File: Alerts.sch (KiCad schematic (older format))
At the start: 26 parts, among them J602 Lights, Q601 bss138, Q602 mac97a8, Q603 bss138, Q604 bss138, Q605 mac97a8, Q606 bss138, Q607 mac97a8, U601 4N35, U602 4N35, U603 4N35

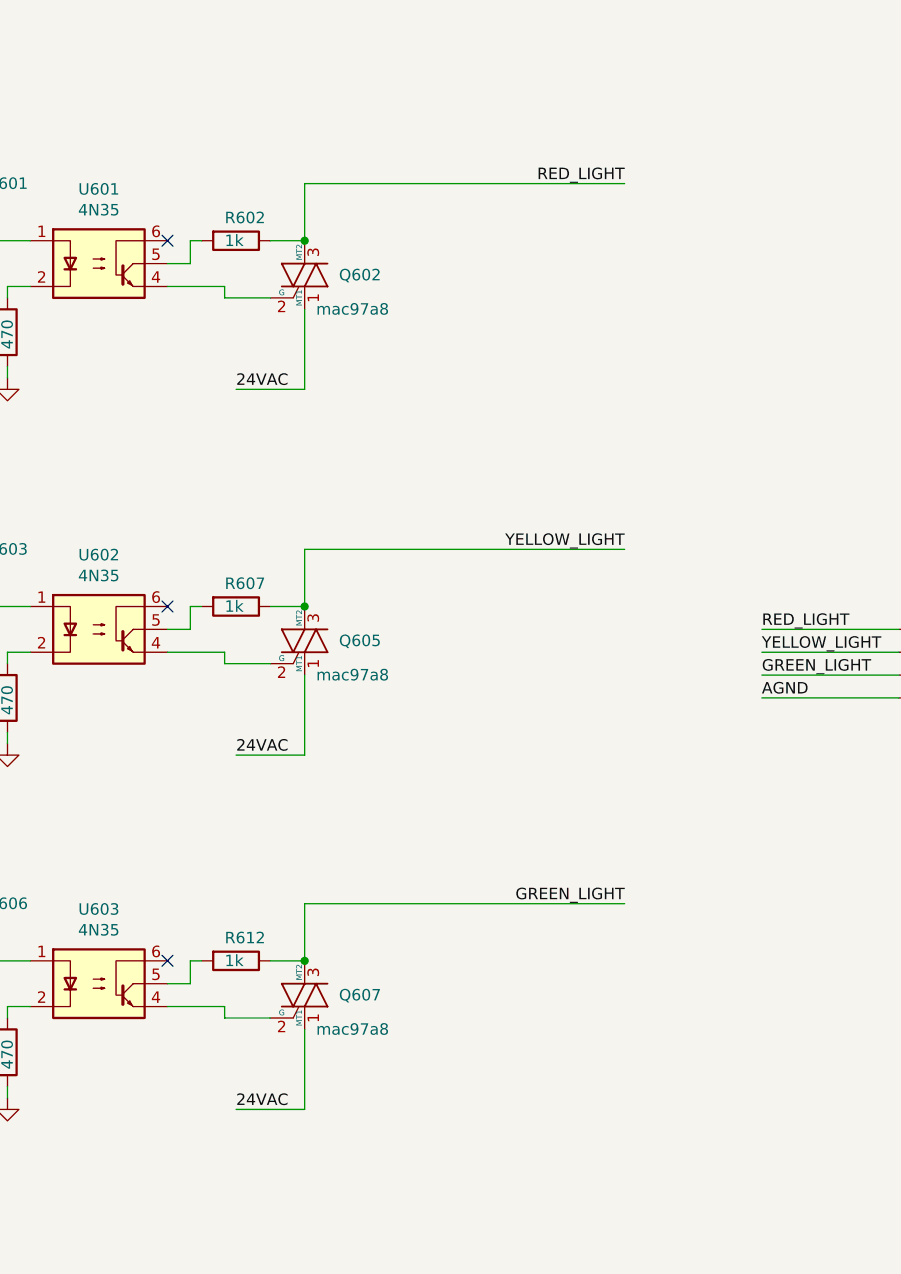
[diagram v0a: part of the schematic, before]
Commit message: Fix por revision grupal
    *Fix de memoria de i2c, mal sda y scl
    *Fix inpunts sda y scl
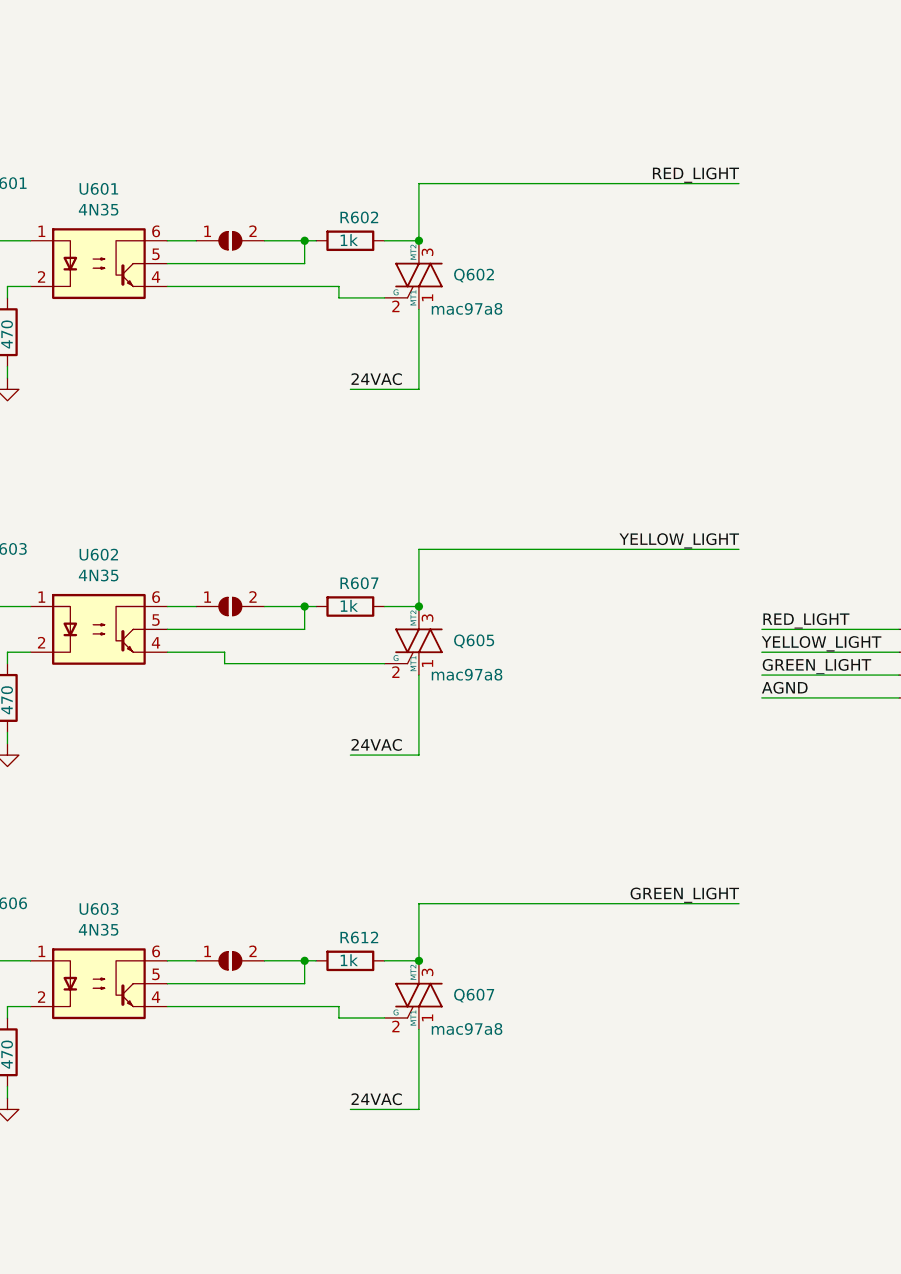
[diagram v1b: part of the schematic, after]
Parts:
- added JP601, JP602, JP603: jumper, 00_lib_fp:SolderJumper-2_P1.3mm_Open_RoundedPad1.0x1.5mm, symbol 00_lib_sch:jumper
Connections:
- net at R602.2, U601.5: now also JP601.2 (B)
- net at U601.6: now also JP601.1 (A)
- net at R607.2, U602.5: now also JP602.2 (B)
- net at U602.6: now also JP602.1 (A)
- net at R612.2, U603.5: now also JP603.2 (B)
- net at U603.6: now also JP603.1 (A)
- no-connect marks 3 -> 0
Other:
- moved on the sheet: Q602, Q605, Q607, R602, R607, R612
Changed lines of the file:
@@
 L 00_lib_sch:Mac97a8 Q?
 U 1 1 616FE40F
-P 7000 1850
+P 7500 1850
 AR Path="/616FE40F" Ref="Q?"  Part="1"
 AR Path="/61410FC3/616FE40F" Ref="Q?"  Part="1"
 AR Path="/61434A7C/616FE40F" Ref="Q?"  Part="1"
 AR Path="/6165BF0A/616FE40F" Ref="Q602"  Part="1"
-F 0 "Q602" H 7150 1850 50  0000 L CNN
-F 1 "mac97a8" H 7050 1700 50  0000 L CNN
-F 2 "00_lib_fp:TO-92_Inline" H 7200 1775 50  0001 L CIN
-F 3 "" H 7000 1850 50  0001 L CNN
-	1    7000 1850
+F 0 "Q602" H 7650 1850 50  0000 L CNN
+F 1 "mac97a8" H 7550 1700 50  0000 L CNN
+F 2 "00_lib_fp:TO-92_Inline" H 7700 1775 50  0001 L CIN
+F 3 "" H 7500 1850 50  0001 L CNN
+	1    7500 1850
 	1    0    0    -1
 $EndComp
@@
 L 00_lib_sch:R R602
 U 1 1 616FE43D
-P 6700 1700
-F 0 "R602" V 6600 1650 50  0000 L CNN
-F 1 "1k" V 6700 1650 50  0000 L CNN
-F 2 "00_lib_fp:R_0805_2012Metric_Pad1.20x1.40mm_HandSolder" V 6630 1700 50  0001 C CNN
-F 3 "~" H 6700 1700 50  0001 C CNN
-	1    6700 1700
+P 7200 1700
+F 0 "R602" V 7100 1650 50  0000 L CNN
+F 1 "1k" V 7200 1650 50  0000 L CNN
+F 2 "00_lib_fp:R_0805_2012Metric_Pad1.20x1.40mm_HandSolder" V 7130 1700 50  0001 C CNN
+F 3 "~" H 7200 1700 50  0001 C CNN
+	1    7200 1700
 	0    1    1    0
 $EndComp
-Wire Wire Line
-	6400 1900 6650 1900
 $Comp
 L 00_lib_sch:GND #PWR?
@@
 $EndComp
 Wire Wire Line
-	6850 1700 7000 1700
-Wire Wire Line
-	7000 1700 7000 1450
-Connection ~ 7000 1700
-Wire Wire Line
-	6650 1900 6650 1950
-Wire Wire Line
-	6650 1950 6850 1950
-Wire Wire Line
-	7000 2000 7000 2350
+	7350 1700 7500 1700
+Wire Wire Line
+	7500 1700 7500 1450
+Connection ~ 7500 1700
+Wire Wire Line
+	7150 1900 7150 1950
+Wire Wire Line
+	7150 1950 7350 1950
+Wire Wire Line
+	7500 2000 7500 2350
 Wire Wire Line
 	5500 2300 5500 2250
@@
 L 00_lib_sch:Mac97a8 Q?
 U 1 1 61703A19
-P 7000 3450
+P 7500 3450
 AR Path="/61703A19" Ref="Q?"  Part="1"
 AR Path="/61410FC3/61703A19" Ref="Q?"  Part="1"
 AR Path="/61434A7C/61703A19" Ref="Q?"  Part="1"
 AR Path="/6165BF0A/61703A19" Ref="Q605"  Part="1"
-F 0 "Q605" H 7150 3450 50  0000 L CNN
-F 1 "mac97a8" H 7050 3300 50  0000 L CNN
-F 2 "00_lib_fp:TO-92_Inline" H 7200 3375 50  0001 L CIN
-F 3 "" H 7000 3450 50  0001 L CNN
-	1    7000 3450
+F 0 "Q605" H 7650 3450 50  0000 L CNN
+F 1 "mac97a8" H 7550 3300 50  0000 L CNN
+F 2 "00_lib_fp:TO-92_Inline" H 7700 3375 50  0001 L CIN
+F 3 "" H 7500 3450 50  0001 L CNN
+	1    7500 3450
 	1    0    0    -1
 $EndComp
@@
 L 00_lib_sch:R R607
 U 1 1 61703A47
-P 6700 3300
-F 0 "R607" V 6600 3250 50  0000 L CNN
-F 1 "1k" V 6700 3250 50  0000 L CNN
-F 2 "00_lib_fp:R_0805_2012Metric_Pad1.20x1.40mm_HandSolder" V 6630 3300 50  0001 C CNN
-F 3 "~" H 6700 3300 50  0001 C CNN
-	1    6700 3300
+P 7200 3300
+F 0 "R607" V 7100 3250 50  0000 L CNN
+F 1 "1k" V 7200 3250 50  0000 L CNN
+F 2 "00_lib_fp:R_0805_2012Metric_Pad1.20x1.40mm_HandSolder" V 7130 3300 50  0001 C CNN
+F 3 "~" H 7200 3300 50  0001 C CNN
+	1    7200 3300
 	0    1    1    0
 $EndComp
@@
 $EndComp
 Wire Wire Line
-	6850 3300 7000 3300
-Wire Wire Line
-	7000 3300 7000 3050
-Connection ~ 7000 3300
+	7350 3300 7500 3300
+Wire Wire Line
+	7500 3300 7500 3050
+Connection ~ 7500 3300
 Wire Wire Line
 	6650 3500 6650 3550
 Wire Wire Line
-	6650 3550 6850 3550
-Wire Wire Line
-	7000 3600 7000 3950
+	7500 3600 7500 3950
 Wire Wire Line
 	5500 3900 5500 3850
@@
 L 00_lib_sch:Mac97a8 Q?
 U 1 1 61705EA7
-P 7000 5000
+P 7500 5000
 AR Path="/61705EA7" Ref="Q?"  Part="1"
 AR Path="/61410FC3/61705EA7" Ref="Q?"  Part="1"
 AR Path="/61434A7C/61705EA7" Ref="Q?"  Part="1"
 AR Path="/6165BF0A/61705EA7" Ref="Q607"  Part="1"
-F 0 "Q607" H 7150 5000 50  0000 L CNN
-F 1 "mac97a8" H 7050 4850 50  0000 L CNN
-F 2 "00_lib_fp:TO-92_Inline" H 7200 4925 50  0001 L CIN
-F 3 "" H 7000 5000 50  0001 L CNN
-	1    7000 5000
+F 0 "Q607" H 7650 5000 50  0000 L CNN
+F 1 "mac97a8" H 7550 4850 50  0000 L CNN
+F 2 "00_lib_fp:TO-92_Inline" H 7700 4925 50  0001 L CIN
+F 3 "" H 7500 5000 50  0001 L CNN
+	1    7500 5000
 	1    0    0    -1
 $EndComp
@@
 L 00_lib_sch:R R612
 U 1 1 61705ED5
-P 6700 4850
-F 0 "R612" V 6600 4800 50  0000 L CNN
-F 1 "1k" V 6700 4800 50  0000 L CNN
-F 2 "00_lib_fp:R_0805_2012Metric_Pad1.20x1.40mm_HandSolder" V 6630 4850 50  0001 C CNN
-F 3 "~" H 6700 4850 50  0001 C CNN
-	1    6700 4850
+P 7200 4850
+F 0 "R612" V 7100 4800 50  0000 L CNN
+F 1 "1k" V 7200 4800 50  0000 L CNN
+F 2 "00_lib_fp:R_0805_2012Metric_Pad1.20x1.40mm_HandSolder" V 7130 4850 50  0001 C CNN
+F 3 "~" H 7200 4850 50  0001 C CNN
+	1    7200 4850
 	0    1    1    0
 $EndComp
-Wire Wire Line
-	6400 5050 6650 5050
 Text HLabel 1450 7250 0    50   Input ~ 0
 [24VAC_alerts]
@@
 $EndComp
 Wire Wire Line
-	6850 4850 7000 4850
-Wire Wire Line
-	7000 4850 7000 4600
-Connection ~ 7000 4850
-Wire Wire Line
-	6650 5050 6650 5100
-Wire Wire Line
-	6650 5100 6850 5100
-Wire Wire Line
-	7000 5150 7000 5500
+	7350 4850 7500 4850
+Wire Wire Line
+	7500 4850 7500 4600
+Connection ~ 7500 4850
+Wire Wire Line
+	7150 5050 7150 5100
+Wire Wire Line
+	7150 5100 7350 5100
+Wire Wire Line
+	7500 5150 7500 5500
 Wire Wire Line
 	5500 5450 5500 5400
@@
 	1    0    0    -1
 $EndComp
-Text Label 8400 3050 2    50   ~ 0
+Text Label 8900 3050 2    50   ~ 0
 YELLOW_LIGHT
-Text Label 8400 4600 2    50   ~ 0
+Text Label 8900 4600 2    50   ~ 0
 GREEN_LIGHT
-Text Label 8400 1450 2    50   ~ 0
+Text Label 8900 1450 2    50   ~ 0
 RED_LIGHT
 Text Label 9000 3400 0    50   ~ 0
@@
 	9000 3600 9600 3600
 Wire Wire Line
-	7000 1450 8400 1450
-Wire Wire Line
-	7000 3050 8400 3050
-Wire Wire Line
-	7000 4600 8400 4600
+	7500 1450 8900 1450
+Wire Wire Line
+	7500 3050 8900 3050
+Wire Wire Line
+	7500 4600 8900 4600
 Text Notes 550  950  0    276  Italic 55
 ALERTS
@@
 Wire Wire Line
 	2000 7250 1450 7250
-Text Label 6700 5500 0    50   ~ 0
+Text Label 7200 5500 0    50   ~ 0
 24VAC
-Text Label 6700 3950 0    50   ~ 0
+Text Label 7200 3950 0    50   ~ 0
 24VAC
 Wire Wire Line
-	6700 3950 7000 3950
-Wire Wire Line
-	6700 5500 7000 5500
-Text Label 6700 2350 0    50   ~ 0
+	7200 3950 7500 3950
+Wire Wire Line
+	7200 5500 7500 5500
+Text Label 7200 2350 0    50   ~ 0
 24VAC
 Wire Wire Line
-	7000 2350 6700 2350
+	7500 2350 7200 2350
 Wire Wire Line
 	9000 3700 9600 3700
@@
 $EndComp
 Wire Wire Line
-	6400 1800 6500 1800
-Wire Wire Line
-	6500 1800 6500 1700
-Wire Wire Line
-	6500 1700 6550 1700
-NoConn ~ 6400 1700
+	7000 1800 7000 1700
+Wire Wire Line
+	7000 1700 7050 1700
 $Comp
 L Isolator:4N35 U602
@@
 $EndComp
 Wire Wire Line
-	6400 3400 6500 3400
-Wire Wire Line
-	6500 3400 6500 3300
-Wire Wire Line
-	6500 3300 6550 3300
-NoConn ~ 6400 3300
+	7000 3400 7000 3300
+Wire Wire Line
+	7000 3300 7050 3300
 $Comp
 L Isolator:4N35 U603
@@
 $EndComp
 Wire Wire Line
-	6400 4950 6500 4950
-Wire Wire Line
-	6500 4950 6500 4850
-Wire Wire Line
-	6500 4850 6550 4850
-NoConn ~ 6400 4850
+	7000 4950 7000 4850
+Wire Wire Line
+	7000 4850 7050 4850
+$Comp
+L 00_lib_sch:jumper JP602
+U 1 1 61909D95
+P 6675 3300
+F 0 "JP602" H 6675 3505 50  0001 C CNN
+F 1 "jumper" H 6675 3414 50  0001 C CNN
+F 2 "00_lib_fp:SolderJumper-2_P1.3mm_Open_RoundedPad1.0x1.5mm" H 6675 3300 50  0001 C CNN
+F 3 "~" H 6675 3300 50  0001 C CNN
+	1    6675 3300
+	1    0    0    -1
+$EndComp
+Wire Wire Line
+	6525 3300 6400 3300
+Wire Wire Line
+	6825 3300 7000 3300
+Connection ~ 7000 3300
+Wire Wire Line
+	6400 3400 7000 3400
+$Comp
+L 00_lib_sch:jumper JP601
+U 1 1 6193194B
+P 6675 1700
+F 0 "JP601" H 6675 1905 50  0001 C CNN
+F 1 "jumper" H 6675 1814 50  0001 C CNN
+F 2 "00_lib_fp:SolderJumper-2_P1.3mm_Open_RoundedPad1.0x1.5mm" H 6675 1700 50  0001 C CNN
+F 3 "~" H 6675 1700 50  0001 C CNN
+	1    6675 1700
+	1    0    0    -1
+$EndComp
+Wire Wire Line
+	6525 1700 6400 1700
+Wire Wire Line
+	6825 1700 7000 1700
+Connection ~ 7000 1700
+Wire Wire Line
+	6400 1800 7000 1800
+Wire Wire Line
+	6400 1900 7150 1900
+Wire Wire Line
+	6400 4950 7000 4950
+Wire Wire Line
+	6400 5050 7150 5050
+Wire Wire Line
+	6650 3550 7350 3550
+$Comp
+L 00_lib_sch:jumper JP603
+U 1 1 6194F7F5
+P 6675 4850
+F 0 "JP603" H 6675 5055 50  0001 C CNN
+F 1 "jumper" H 6675 4964 50  0001 C CNN
+F 2 "00_lib_fp:SolderJumper-2_P1.3mm_Open_RoundedPad1.0x1.5mm" H 6675 4850 50  0001 C CNN
+F 3 "~" H 6675 4850 50  0001 C CNN
+	1    6675 4850
+	1    0    0    -1
+$EndComp
+Wire Wire Line
+	6525 4850 6400 4850
+Wire Wire Line
+	6825 4850 7000 4850
+Connection ~ 7000 4850
 $EndSCHEMATC
